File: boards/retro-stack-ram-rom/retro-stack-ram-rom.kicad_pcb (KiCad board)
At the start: 2 copper layers, 99.1 x 99.1 mm, 29 parts, among them J1 BUS_6502, J2 TRM_PWR, J3 PLD_RR_CTL, J4 RR_CTL, J5 SMP_RR_CTL, U1 74HC00, U2 28C256, U3 AS6C62256, U4 ATF16V8B-15PU

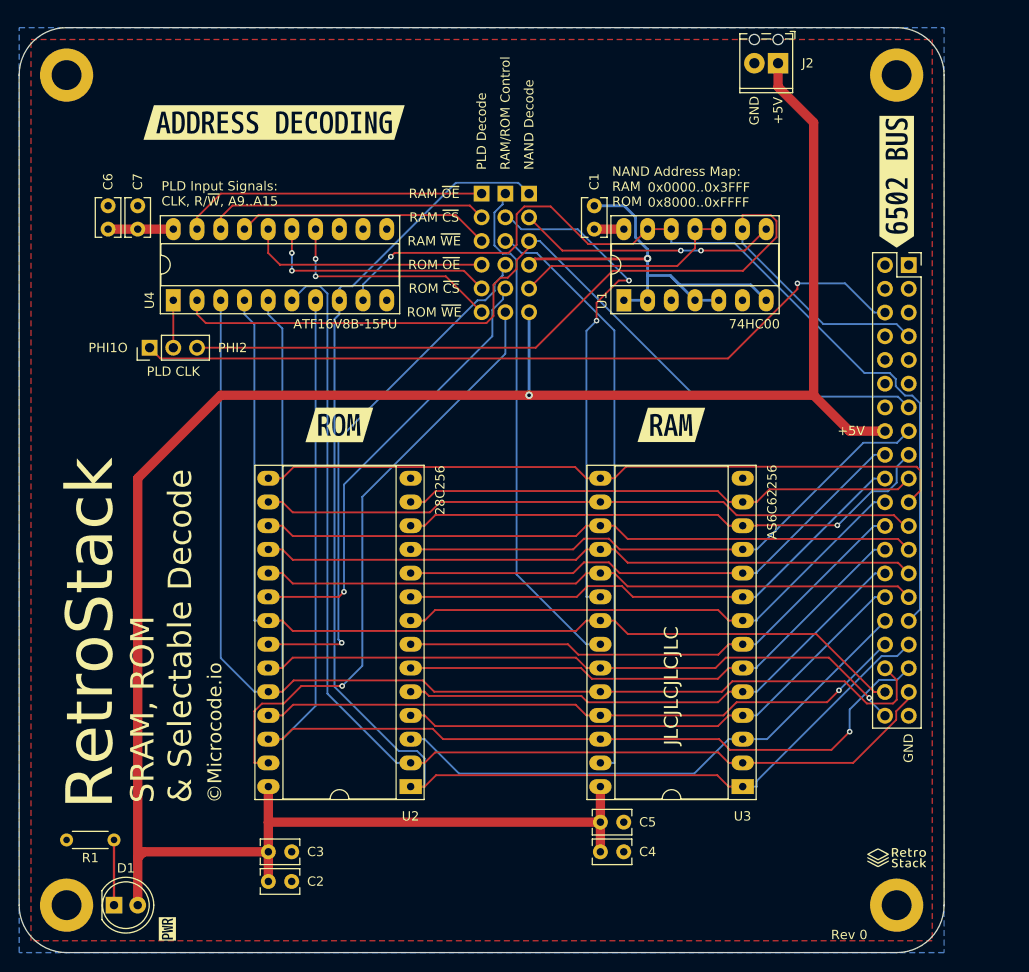
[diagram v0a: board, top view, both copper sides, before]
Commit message: Update ram/rom to only use pld.
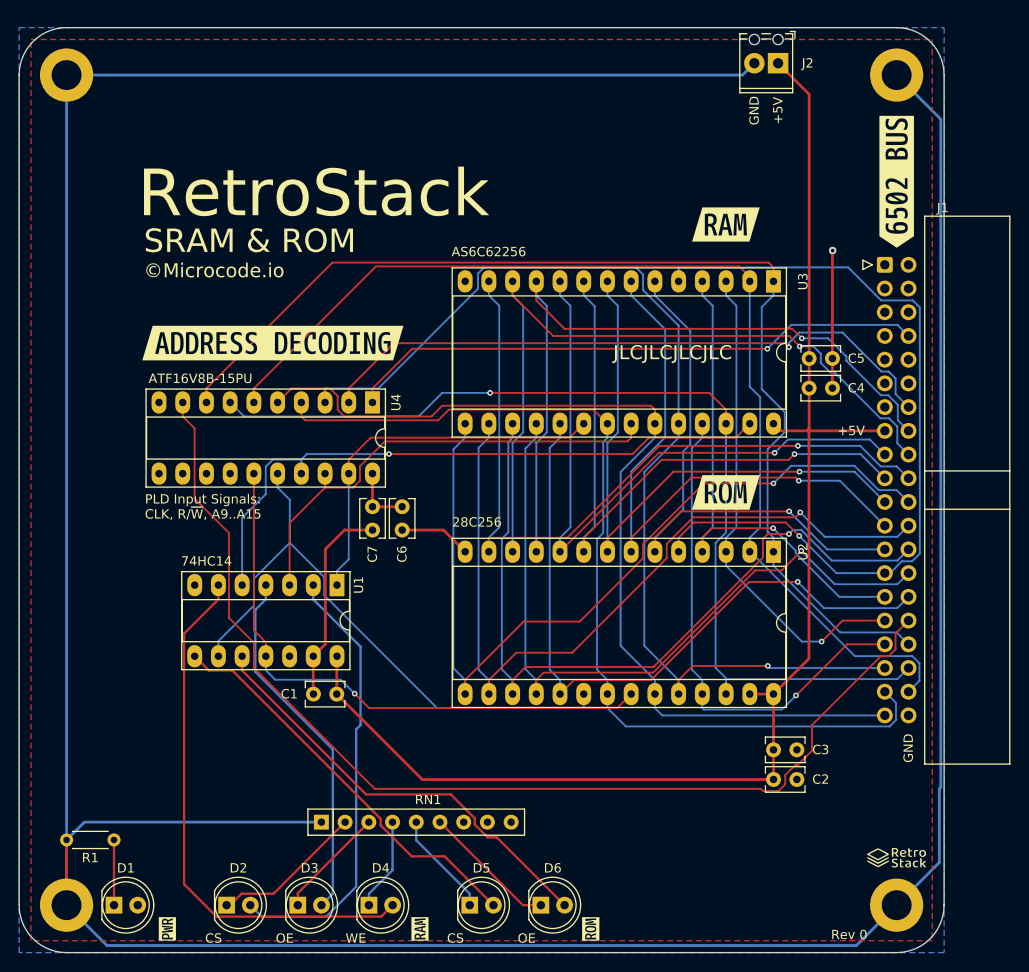
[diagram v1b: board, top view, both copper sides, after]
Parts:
- removed J3: PLD_RR_CTL, Connector_PinHeader_2.54mm:PinHeader_1x06_P2.54mm_Vertical
- removed J4: RR_CTL, Connector_PinHeader_2.54mm:PinHeader_1x06_P2.54mm_Vertical
- removed J5: SMP_RR_CTL, Connector_PinHeader_2.54mm:PinHeader_1x06_P2.54mm_Vertical
- removed JP1: JMP_PLDCK, Connector_PinHeader_2.54mm:PinHeader_1x03_P2.54mm_Vertical
- added D2: LED, LED_THT:LED_D5.0mm, F.Cu at (123.8, 132.1)
- added D3: LED, LED_THT:LED_D5.0mm, F.Cu at (131.4, 132.1)
- added D4: LED, LED_THT:LED_D5.0mm, F.Cu at (139.1, 132.1)
- added D5: LED, LED_THT:LED_D5.0mm, F.Cu at (149.9, 132.1)
- added D6: LED, LED_THT:LED_D5.0mm, F.Cu at (157.5, 132.1)
- added RN1: 1k, Resistor_THT:R_Array_SIP9, F.Cu at (134.0, 123.2)
- added kibuzzard-6448402D: G***, kibuzzard-6448402D, F.Cu at (144.5, 134.6)
- added kibuzzard-64484043: G***, kibuzzard-64484043, F.Cu at (162.8, 134.6)
- J1: footprint Connector_PinSocket_2.54mm:PinSocket_2x20_P2.54mm_Vertical -> Connector_IDC:IDC-Header_2x20_P2.54mm_Horizontal
- U1: value 74HC00 -> 74HC14
- moved C1 56.9 mm to (135.6, 109.5), turned to 180 degrees
- moved C2 55.2 mm to (182.4, 118.6)
- moved C3 55.2 mm to (182.4, 115.4)
- moved C4 54.5 mm to (186.2, 76.7)
- moved C5 54.5 mm to (186.2, 73.5)
- moved U3 54.2 mm to (182.4, 65.3), turned to -90 degrees
- moved U2 46.3 mm to (182.4, 94.2), turned to -90 degrees
- moved C6 43.3 mm to (142.6, 89.4), turned to -90 degrees
- moved U1 43.3 mm to (135.6, 97.8), turned to -90 degrees
- moved kibuzzard-642DBD4D 42.0 mm to (177.3, 87.9)
- moved C7 38.9 mm to (139.4, 89.4), turned to -90 degrees
- moved U4 24.0 mm to (139.4, 78.2), turned to -90 degrees
- moved kibuzzard-642DC482 23.6 mm to (128.8, 71.9)
- moved kibuzzard-642DBD42 22.2 mm to (177.3, 59.2)
- moved J1 2.56 mm to (194.3, 63.5)
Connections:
- J1 pad 1: /~{RES} -> /VPB
- J1 pad 10: /~{ML} -> /BE
- J1 pad 11: /NC -> /~{NMI}
- J1 pad 12: /~{NMI} -> /NC
- J1 pad 13: /R/~{W} -> /SYNC
- J1 pad 14: /SYNC -> /R/~{W}
- J1 pad 15: /D0 -> +5V
- J1 pad 16: +5V -> /D0
- J1 pad 17: /D1 -> /A0
- J1 pad 18: /A0 -> /D1
- J1 pad 19: /D2 -> /A1
- J1 pad 2: /VPB -> /~{RES}
- J1 pad 20: /A1 -> /D2
- J1 pad 21: /D3 -> /A2
- J1 pad 22: /A2 -> /D3
- J1 pad 23: /D4 -> /A3
- J1 pad 24: /A3 -> /D4
- J1 pad 25: /D5 -> /A4
- J1 pad 26: /A4 -> /D5
- J1 pad 27: /D6 -> /A5
- J1 pad 28: /A5 -> /D6
- J1 pad 29: /D7 -> /A6
- J1 pad 3: /PHI2O -> /RDY
- J1 pad 30: /A6 -> /D7
- J1 pad 31: /A15 -> /A7
- J1 pad 32: /A7 -> /A15
- J1 pad 33: /A14 -> /A8
- J1 pad 34: /A8 -> /A14
- J1 pad 35: /A13 -> /A9
- J1 pad 36: /A9 -> /A13
- J1 pad 37: /A12 -> /A10
- J1 pad 38: /A10 -> /A12
- J1 pad 39: GND -> /A11
- J1 pad 4: /RDY -> /PHI2O
- J1 pad 40: /A11 -> GND
- J1 pad 5: /~{SO} -> /PHI1O
- J1 pad 6: /PHI1O -> /~{SO}
- J1 pad 7: /PHI2 -> /~{IRQ}
- J1 pad 8: /~{IRQ} -> /PHI2
- J1 pad 9: /BE -> /~{ML}
- U1 pad 1: GND -> /RAM_~{CS}
- U1 pad 10: /~{A15} -> Net-(D6-Pad2)
- U1 pad 11: /~{A15} -> /ROM_~{OE}
- U1 pad 12: /A15 -> unconnected-(U1-Pad12)
- U1 pad 13: /A15 -> GND
- U1 pad 2: GND -> Net-(D2-Pad2)
- U1 pad 3: unconnected-(U1-Pad3) -> /RAM_~{OE}
- U1 pad 4: GND -> Net-(D3-Pad2)
- U1 pad 5: GND -> /RAM_~{WE}
- U1 pad 6: unconnected-(U1-Pad6) -> Net-(D4-Pad2)
- U1 pad 8: /SMP_RAM_~{CS} -> Net-(D5-Pad2)
- U1 pad 9: /PHI2 -> /ROM_~{CS}
- U2 pad 27: /ROM_~{WE} -> +5V
- U4 pad 1: /PLDCK -> /PHI2
- U4 pad 14: /PLD_ROM_~{WE} -> unconnected-(U4-Pad14)
- U4 pad 15: /PLD_ROM_~{CS} -> /ROM_~{OE}
- U4 pad 16: /PLD_ROM_~{OE} -> /ROM_~{CS}
- U4 pad 17: /PLD_RAM_~{WE} -> /RAM_~{WE}
- U4 pad 18: /PLD_RAM_~{CS} -> /RAM_~{OE}
- U4 pad 19: /PLD_RAM_~{OE} -> /RAM_~{CS}
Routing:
- net GND: track 50.0 -> 427.9 mm
- net +5V: track 254.2 -> 155.8 mm, vias 1 -> 0
- net /PHI1O: track 84.2 -> 0.00 mm, vias 1 -> 0
- net /ROM_~{WE}: track 64.8 -> 0.00 mm, vias 1 -> 0
- net Net-(D4-Pad2): track 0.00 -> 57.8 mm
- net Net-(D2-Pad2): track 0.00 -> 47.8 mm
- net Net-(D6-Pad2): track 0.00 -> 46.9 mm
- net Net-(D5-Pad2): track 0.00 -> 43.4 mm
- net Net-(D3-Pad2): track 0.00 -> 38.7 mm
- net /PHI2: track 97.5 -> 62.2 mm, vias 0 -> 1
- net /PLD_RAM_~{OE}: track 32.8 -> 0.00 mm
- net /PLD_RAM_~{CS}: track 30.2 -> 0.00 mm
- net /A5: track 57.0 -> 86.6 mm, vias 0 -> 1
- net /SMP_RAM_~{CS}: track 27.8 -> 0.00 mm, vias 2 -> 0
- net /PLD_RAM_~{WE}: track 27.2 -> 0.00 mm
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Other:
- board text added: "CS"
- board text added: "OE"
- board text added: "SRAM & ROM"
- board text added: "WE"
- board text removed: "0x0000..0x3FFF 0x8000..0xFFFF"
- board text removed: "NAND Address Map: RAM ROM"
- board text removed: "NAND Decode"
- board text removed: "PHI1O"
- board text removed: "PHI2"
- board text removed: "PLD CLK"
- board text removed: "PLD Decode"
- board text removed: "RAM ~{CS}"
- board text removed: "RAM ~{OE}"
- board text removed: "RAM ~{WE}"
- board text removed: "RAM/ROM Control"
- board text removed: "ROM ~{CS}"
- board text removed: "ROM ~{OE}"
- board text removed: "ROM ~{WE}"
- board text removed: "SRAM, ROM & Selectable Decode"

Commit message: Initial PLD test and RAM/ROM board.
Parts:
- removed R1: 1k, Resistor_THT:R_Axial_DIN0204_L3.6mm_D1.6mm_P5.08mm_Horizontal
- U2: footprint Package_DIP:DIP-28_W15.24mm_Socket_LongPads -> RetroStack:28655410
- moved U1 54.2 mm to (184.7, 120.9)
- moved C1 54.2 mm to (184.6, 132.6)
- moved C4 43.0 mm to (145.3, 63.5), turned to 180 degrees
- moved C3 42.9 mm to (149.1, 88.4), turned to 90 degrees
- moved C2 42.7 mm to (152.3, 88.4), turned to 90 degrees
- moved C5 41.5 mm to (145.3, 66.7), turned to 180 degrees
- moved U3 37.3 mm to (148.3, 80.5), turned to 90 degrees
- moved U2 34.9 mm to (151.1, 109.7), turned to 0 degrees
- moved C6 6.77 mm to (135.9, 88.6)
- moved C7 6.77 mm to (132.7, 88.6)
- moved kibuzzard-642DC482 5.85 mm to (122.9, 71.6)
- moved U4 5.09 mm to (134.4, 78.0)
- moved D1 2.80 mm to (114.6, 132.1), turned to 180 degrees
- moved kibuzzard-642DBD42 1.78 mm to (177.3, 61.0)
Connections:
- D1 pad 1: Net-(D1-Pad1) -> /PWR_R
- D2 pad 1: Net-(D2-Pad1) -> Net-(RN1-Pad3)
- D3 pad 1: Net-(D3-Pad1) -> Net-(RN1-Pad4)
- D4 pad 1: Net-(D4-Pad1) -> Net-(RN1-Pad5)
- D5 pad 1: Net-(D5-Pad1) -> Net-(RN1-Pad6)
- D6 pad 1: Net-(D6-Pad1) -> Net-(RN1-Pad7)
- RN1 pad 2: Net-(D2-Pad1) -> /PWR_R
- RN1 pad 3: Net-(D3-Pad1) -> Net-(RN1-Pad3)
- RN1 pad 4: Net-(D4-Pad1) -> Net-(RN1-Pad4)
- RN1 pad 5: Net-(D5-Pad1) -> Net-(RN1-Pad5)
- RN1 pad 6: Net-(D6-Pad1) -> Net-(RN1-Pad6)
- RN1 pad 7: unconnected-(RN1-Pad7) -> Net-(RN1-Pad7)
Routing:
- net GND: track 427.9 -> 224.6 mm
- net /RAM_~{CS}: track 40.7 -> 142.8 mm, vias 0 -> 1
- net /RAM_~{OE}: track 50.9 -> 113.0 mm, vias 0 -> 2
- net /D3: track 91.0 -> 42.6 mm, vias 1 -> 0
- net /RAM_~{WE}: track 69.0 -> 108.4 mm, vias 1 -> 0
- net /D4: track 86.2 -> 48.1 mm, vias 1 -> 0
- net /A13: track 106.9 -> 142.1 mm
- net /D5: track 83.5 -> 49.3 mm, vias 1 -> 0
- net /D2: track 81.8 -> 47.9 mm
- net +5V: track 155.8 -> 186.5 mm, vias 0 -> 3
- net Net-(D6-Pad2): track 46.9 -> 16.9 mm
- net /D1: track 82.5 -> 53.6 mm, vias 1 -> 0
- net /D6: track 79.0 -> 51.5 mm, vias 1 -> 0
- net /ROM_~{CS}: track 64.7 -> 92.1 mm, vias 0 -> 2
- net /ROM_~{OE}: track 63.0 -> 89.9 mm, vias 1 -> 0
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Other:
- board text added: "Input Signals: CLK, R/~{W}, A9..A15"
- board text added: "Output Signals: RAM ~{CS}, ~{OE}, ~{WE} ROM ~{CS}, ~{OE}"
- board text added: "SRAM & EEPROM"
- board text removed: "PLD Input Signals: CLK, R/~{W}, A9..A15"
- board text removed: "SRAM & ROM"
